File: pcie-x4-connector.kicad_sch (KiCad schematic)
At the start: 13 parts, among them J10 Bus_M.2_1-2199230-6, Y5 Oscillator_32.768kHz_ECS_2520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

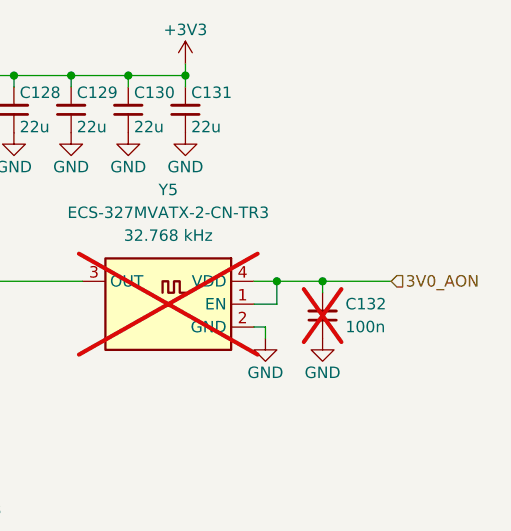
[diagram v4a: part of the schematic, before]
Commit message: [#83767] Power Y5 from 3.3V rail
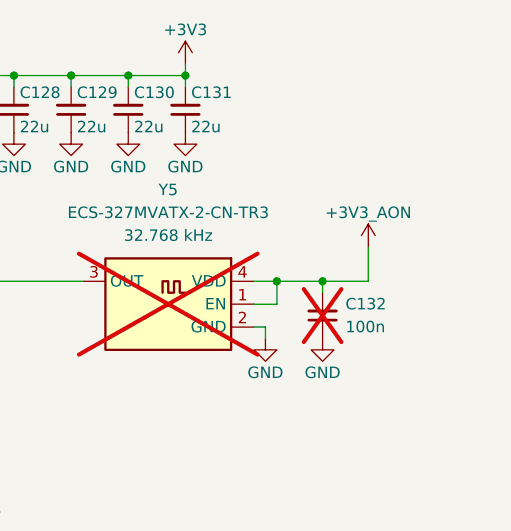
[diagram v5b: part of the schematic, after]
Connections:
- net 3V0_AON renamed +3V3_AON
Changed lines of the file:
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@@
+	)
+	(junction
+		(at 190.5 90.17)
+		(diameter 0)
+		(color 0 0 0 0)
+	)
+	(junction
+		(at 236.22 88.9)
+		(diameter 0)
+		(color 0 0 0 0)
+	)
+	(junction
+		(at 226.06 176.53)
+		(diameter 0)
+		(color 0 0 0 0)
 	)
 	(junction
@@
 	)
 	(junction
-		(at 190.5 90.17)
-		(diameter 0)
-		(color 0 0 0 0)
-	)
-	(junction
-		(at 236.22 88.9)
-		(diameter 0)
-		(color 0 0 0 0)
-	)
-	(junction
-		(at 226.06 176.53)
-		(diameter 0)
-		(color 0 0 0 0)
-	)
-	(junction
 		(at 248.92 88.9)
 		(diameter 0)
@@
 		)
 	)
+	(wire
+		(pts
+			(xy 269.24 111.76) (xy 264.16 111.76)
+		)
+		(stroke
+			(width 0)
+			(type default)
+		)
+	)
 	(bus
 		(pts
@@
 	(wire
 		(pts
-			(xy 264.16 111.76) (xy 271.78 111.76)
+			(xy 269.24 107.95) (xy 269.24 111.76)
 		)
 		(stroke
@@
 			)
 			(justify right)
-		)
-	)
-	(hierarchical_label "3V0_AON"
-		(shape input)
-		(at 271.78 111.76 0)
-		(effects
-			(font
-				(size 1.27 1.27)
-			)
-			(justify left)
 		)
 	)
@@
 					(unit 1)
 				)
+			)
+		)
+	)
+	(symbol
+		(lib_id "antmicropower:+3V3_AON")
+		(at 269.24 107.95 0)
+		(unit 1)
+		(exclude_from_sim no)
+		(in_bom yes)
+		(on_board yes)
+		(dnp no)
+		(property "Reference" "#PWR040"
+			(at 269.24 111.76 0)
+			(effects
+				(font
+					(size 1.27 1.27)
+				)
+				(hide yes)
+			)
+		)
+		(property "Value" "+3V3_AON"
+			(at 269.24 104.14 0)
+			(effects
+				(font
+					(size 1.27 1.27)
+				)
+			)
+		)
+		(property "Footprint" ""
+			(at 269.24 107.95 0)
+			(effects
+				(font
+					(size 1.27 1.27)
+				)
+				(hide yes)
+			)
+		)
+		(property "Datasheet" ""
+			(at 269.24 107.95 0)
+			(effects
+				(font
+					(size 1.27 1.27)
+				)
+				(hide yes)
+			)
+		)
+		(property "Description" ""
+			(at 269.24 107.95 0)
+			(effects
+				(font
+					(size 1.27 1.27)
+				)
+				(hide yes)
+			)
+		)
+		(pin "1"
+		)
+		(instances
+			(project "bmc-reference-carrier-board"
+				(path "/5f636c45-3c15-4731-8931-4625e0dab7e4/945730c0-5d04-4966-88eb-4ee840f8c440"
+					(reference "#PWR040")
+					(unit 1)
+				)

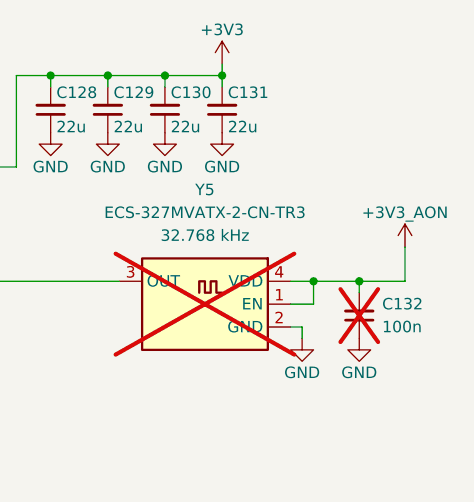
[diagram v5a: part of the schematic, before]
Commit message: [#83767] Add SGMII RX/TX swap note
Fix signal level on U26 SEL pin
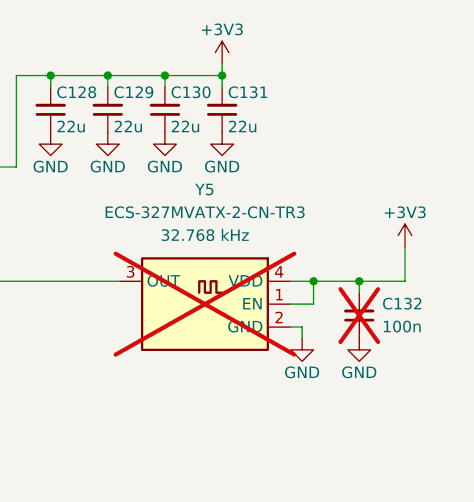
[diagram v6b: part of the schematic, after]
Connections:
- net +3V3_AON is gone; now on net +3V3: C132.2, Y5.1 (EN), Y5.4 (VDD)
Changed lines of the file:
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@@
-	)
-	(symbol
-		(lib_id "antmicropower:+3V3_AON")
-		(at 269.24 107.95 0)
-		(unit 1)
-		(exclude_from_sim no)
-		(in_bom yes)
-		(on_board yes)
-		(dnp no)
-		(property "Reference" "#PWR040"
-			(at 269.24 111.76 0)
-			(effects
-				(font
-					(size 1.27 1.27)
-				)
-				(hide yes)
-			)
-		)
-		(property "Value" "+3V3_AON"
-			(at 269.24 104.14 0)
-			(effects
-				(font
-					(size 1.27 1.27)
-				)
-			)
-		)
-		(property "Footprint" ""
-			(at 269.24 107.95 0)
-			(effects
-				(font
-					(size 1.27 1.27)
-				)
-				(hide yes)
-			)
-		)
-		(property "Datasheet" ""
-			(at 269.24 107.95 0)
-			(effects
-				(font
-					(size 1.27 1.27)
-				)
-				(hide yes)
-			)
-		)
-		(property "Description" ""
-			(at 269.24 107.95 0)
-			(effects
-				(font
-					(size 1.27 1.27)
-				)
-				(hide yes)
-			)
-		)
-		(pin "1"
-		)
-		(instances
-			(project "bmc-reference-carrier-board"
-				(path "/5f636c45-3c15-4731-8931-4625e0dab7e4/945730c0-5d04-4966-88eb-4ee840f8c440"
-					(reference "#PWR040")
-					(unit 1)
-				)
-			)
-		)
 	)
 	(symbol
@@
 					(unit 1)
 				)
+			)
+		)
+	)
+	(symbol
+		(lib_id "antmicropower:+3V3")
+		(at 269.24 107.95 0)
+		(unit 1)
+		(exclude_from_sim no)
+		(in_bom yes)
+		(on_board yes)
+		(dnp no)
+		(property "Reference" "#PWR0418"
+			(at 284.48 107.95 0)
+			(effects
+				(font
+					(size 1.27 1.27)
+					(thickness 0.15)
+				)
+				(justify left bottom)
+				(hide yes)
+			)
+		)
+		(property "Value" "+3V3"
+			(at 269.24 104.14 0)
+			(effects
+				(font
+					(size 1.27 1.27)
+					(thickness 0.15)
+				)
+			)
+		)
+		(property "Footprint" ""
+			(at 284.48 115.57 0)
+			(effects
+				(font
+					(size 1.27 1.27)
+					(thickness 0.15)
+				)
+				(justify left bottom)
+				(hide yes)
+			)
+		)
+		(property "Datasheet" ""
+			(at 284.48 118.11 0)
+			(effects
+				(font
+					(size 1.27 1.27)
+					(thickness 0.15)
+				)
+				(justify left bottom)
+				(hide yes)
+			)
+		)
+		(property "Description" ""
+			(at 269.24 107.95 0)
+			(effects
+				(font
+					(size 1.27 1.27)
+				)
+				(hide yes)
+			)
+		)
+		(property "Author" "Antmicro"
+			(at 284.48 110.49 0)
+			(effects
+				(font
+					(size 1.27 1.27)
+					(thickness 0.15)
+				)
+				(justify left bottom)
+				(hide yes)
+			)
+		)
+		(property "License" "Apache-2.0"
+			(at 284.48 113.03 0)
+			(effects
+				(font
+					(size 1.27 1.27)
+					(thickness 0.15)
+				)
+				(justify left bottom)
+				(hide yes)
+			)
+		)
+		(pin "1"
+		)
+		(instances
+			(project "bmc-reference-carrier-board"
+				(path "/5f636c45-3c15-4731-8931-4625e0dab7e4/945730c0-5d04-4966-88eb-4ee840f8c440"
+					(reference "#PWR0418")
+					(unit 1)
+				)

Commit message: [#83767] Disable PCIe x4
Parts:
- removed D12: LED_G_0603_LTST-C190KGKT, antmicro-footprints:LED_0603_1608Metric_G, symbol antmicroLEDIndicationDiscrete:LED_G_0603_LTST-C190KGKT
- added D12: LED_G_0402_VLMTG1500-GS08, antmicro-footprints:LED_0402_1005Metric_G, symbol antmicroLEDIndicationDiscrete:LED_G_0402_VLMTG1500-GS08
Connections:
- net at J10.10 (LED): now also D12.1 (C)
- net at R241.1: now also D12.2 (A)
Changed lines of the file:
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@@
-	)
-	(symbol
-		(lib_id "antmicroLEDIndicationDiscrete:LED_G_0603_LTST-C190KGKT")
-		(at 226.06 152.4 90)
-		(unit 1)
-		(exclude_from_sim no)
-		(in_bom yes)
-		(on_board yes)
-		(dnp no)
-		(fields_autoplaced yes)
-		(property "Reference" "D12"
-			(at 228.6 148.59 90)
-			(effects
-				(font
-					(size 1.27 1.27)
-					(thickness 0.15)
-				)
-				(justify right)
-			)
-		)
-		(property "Value" "LED_G_0603_LTST-C190KGKT"
-			(at 233.68 129.54 0)
-			(effects
-				(font
-					(size 1.27 1.27)
-					(thickness 0.15)
-				)
-				(justify left bottom)
-				(hide yes)
-			)
-		)
-		(property "Footprint" "antmicro-footprints:LED_0603_1608Metric_G"
-			(at 236.22 129.54 0)
-			(effects
-				(font
-					(size 1.27 1.27)
-					(thickness 0.15)
-				)
-				(justify left bottom)
-				(hide yes)
-			)
-		)
-		(property "Datasheet" "https://optoelectronics.liteon.com/upload/download/DS22-2000-074/LTST-C190KGKT.PDF"
-			(at 238.76 129.54 0)
-			(effects
-				(font
-					(size 1.27 1.27)
-					(thickness 0.15)
-				)
-				(justify left bottom)
-				(hide yes)
-			)
-		)
-		(property "Description" "LED, Green, SMD, 0603, 20 mA, 1.9 V, 571 nm"
-			(at 226.06 152.4 0)
-			(effects
-				(font
-					(size 1.27 1.27)
-				)
-				(hide yes)
-			)
-		)
-		(property "MPN" "LTST-C190KGKT"
-			(at 241.3 129.54 0)
-			(effects
-				(font
-					(size 1.27 1.27)
-					(thickness 0.15)
-				)
-				(justify left bottom)
-				(hide yes)
-			)
-		)
-		(property "Manufacturer" "Lite-On"
-			(at 243.84 129.54 0)
-			(effects
-				(font
-					(size 1.27 1.27)
-					(thickness 0.15)
-				)
-				(justify left bottom)
-				(hide yes)
-			)
-		)
-		(property "Color" "Green"
-			(at 228.6 151.1299 90)
-			(effects
-				(font
-					(size 1.27 1.27)
-				)
-				(justify right)
-			)
-		)
-		(property "Author" "Antmicro"
-			(at 246.38 129.54 0)
-			(effects
-				(font
-					(size 1.27 1.27)
-					(thickness 0.15)
-				)
-				(justify left bottom)
-				(hide yes)
-			)
-		)
-		(property "License" "Apache-2.0"
-			(at 248.92 129.54 0)
-			(effects
-				(font
-					(size 1.27 1.27)
-					(thickness 0.15)
-				)
-				(justify left bottom)
-				(hide yes)
-			)
-		)
-		(pin "2"
-		)
-		(pin "1"
-		)
-		(instances
-			(project ""
-				(path "/5f636c45-3c15-4731-8931-4625e0dab7e4/945730c0-5d04-4966-88eb-4ee840f8c440"
-					(reference "D12")
-					(unit 1)
-				)
-			)
-		)
 	)
 	(symbol
@@
 					(unit 1)
 				)
+			)
+		)
+	)
+	(symbol
+		(lib_id "antmicroLEDIndicationDiscrete:LED_G_0402_VLMTG1500-GS08")
+		(at 226.06 152.4 90)
+		(unit 1)
+		(exclude_from_sim no)
+		(in_bom yes)
+		(on_board yes)
+		(dnp no)
+		(fields_autoplaced yes)
+		(property "Reference" "D12"
+			(at 228.6 148.59 90)
+			(effects
+				(font
+					(size 1.27 1.27)
+					(thickness 0.15)
+				)
+				(justify right)
+			)
+		)
+		(property "Value" "LED_G_0402_VLMTG1500-GS08"
+			(at 233.68 129.54 0)
+			(effects
+				(font
+					(size 1.27 1.27)
+					(thickness 0.15)
+				)
+				(justify left bottom)
+				(hide yes)
+			)
+		)
+		(property "Footprint" "antmicro-footprints:LED_0402_1005Metric_G"
+			(at 236.22 129.54 0)
+			(effects
+				(font
+					(size 1.27 1.27)
+					(thickness 0.15)
+				)
+				(justify left bottom)
+				(hide yes)
+			)
+		)
+		(property "Datasheet" "https://www.vishay.com/docs/82554/vlmo1500.pdf"
+			(at 238.76 129.54 0)
+			(effects
+				(font
+					(size 1.27 1.27)
+					(thickness 0.15)
+				)
+				(justify left bottom)
+				(hide yes)
+			)
+		)
+		(property "Description" "LED, Green, SMD, 1005, 5 mA, 3.1 V, 535 nm"
+			(at 250.698 106.934 0)
+			(effects
+				(font
+					(size 1.27 1.27)
+				)
+				(hide yes)
+			)
+		)
+		(property "MPN" "VLMTG1500-GS08"
+			(at 241.3 129.54 0)
+			(effects
+				(font
+					(size 1.27 1.27)
+					(thickness 0.15)
+				)
+				(justify left bottom)
+				(hide yes)
+			)
+		)
+		(property "Manufacturer" "Vishay"
+			(at 243.84 129.54 0)
+			(effects
+				(font
+					(size 1.27 1.27)
+					(thickness 0.15)
+				)
+				(justify left bottom)
+				(hide yes)
+			)
+		)
+		(property "Color" "Green"
+			(at 228.6 151.1299 90)
+			(effects
+				(font
+					(size 1.27 1.27)
+				)
+				(justify right)
+			)
+		)
+		(property "Author" "Antmicro"
+			(at 246.38 129.54 0)
+			(effects
+				(font
+					(size 1.27 1.27)
+					(thickness 0.15)
+				)
+				(justify left bottom)
+				(hide yes)
+			)
+		)
+		(property "License" "Apache-2.0"
+			(at 248.92 129.54 0)
+			(effects
+				(font
+					(size 1.27 1.27)
+					(thickness 0.15)
+				)
+				(justify left bottom)
+				(hide yes)
+			)
+		)
+		(pin "1"
+		)
+		(pin "2"
+		)
+		(instances
+			(project "bmc-reference-carrier-board"
+				(path "/5f636c45-3c15-4731-8931-4625e0dab7e4/945730c0-5d04-4966-88eb-4ee840f8c440"
+					(reference "D12")
+					(unit 1)
+				)
